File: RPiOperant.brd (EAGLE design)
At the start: 80 x 64 mm, 34 parts, among them IC1 74LS14N, IC3 MCP3008, J2 POWER_JACK, J3 POWER_JACK

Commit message: new board
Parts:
- removed D2: 1N4004, diode:DO41-10
- removed Q2: (no value), adafruit:TO220V
- removed R22, R23: 330, resistor:0207/7
- added IC2: 74LS14N, 74xx-us:DIL14
- added J1, J4: USB_B_PTH, SparkFun-Connectors:USB-B-PTH
- added J5, J6, J7, J8, J9: 1X2-3.5MM, adafruit:1X2-3.5MM
- added Q3, Q4, Q5, Q6: (no value), adafruit:TO220V
- added R24, R25, R26, R27, R28, R29: 1k, resistor:0207/7
- added R30, R31, R32, R33, R34, R35: 4.3k, resistor:0207/7
- added R36, R37, R38: 330, resistor:0207/7
- added U1: (no value), adafruit:TSSOP28
- added X2: (no value), con-subd:F25HP
- R17: value 1k -> 330
- moved R12 142.4 mm to (96.0, 45.0)
- moved R11 129.1 mm to (86.0, 50.0)
- moved SV1 126.0 mm to (131.0, 35.0), turned to 270 degrees
- moved R9 120.1 mm to (106.0, 40.0)
- moved R10 111.9 mm to (86.0, 40.0)
- moved SV2 70.0 mm to (5.00, 34.0), turned to 270 degrees
- moved Q1 64.0 mm to (43.0, 73.0)
- moved IC1 58.8 mm to (66.0, 58.0), turned to 0 degrees
- moved R17 55.8 mm to (96.0, 50.0)
- moved IC3 51.0 mm to (80.0, 28.0), turned to 0 degrees
- moved D1 50.8 mm to (17.0, 67.0), turned to 0 degrees
- moved R16 47.4 mm to (35.0, 67.0)
- moved R14 36.1 mm to (22.0, 43.0)
- moved X1 35.0 mm to (41.0, 88.0)
- moved R2 26.2 mm to (35.0, 58.0), turned to 0 degrees
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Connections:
- removed net GPIO2: SV1.3, SV2.3, X1.14
- removed net GPIO25: X1.18
- removed net GPIO3: SV1.5, SV2.5, X1.15
- removed net GPIO4: SV1.7, SV2.7
- removed net HOPPER_IR_LED: R12.1, X1.19
- removed net HOUSE_LIGHTS: D2.A, Q2.2, X1.5
- removed net IR_LED_C: R10.1, X1.21
- removed net IR_LED_L: R9.1, X1.22
- removed net IR_LED_R: R11.1, X1.20
- removed net LIGHTS_TRIG_GPIO: R17.1, SV1.32, SV2.32
- new net AUX1: J5.1, SV1.7, X2.1
- new net AUX2: J5.2, SV1.32, X2.2
- new net AUX3: J6.1, X2.3
- new net AUX4: J6.2, X2.4
- new net CENTNER_LED: R36.1
- new net GPIO18: J9.2, SV1.12
- new net HOUSELIGHT_B: Q4.2, X1.20
- new net HOUSELIGHT_B_GPIO: Q4.1, U1.8
- new net HOUSELIGHT_G: Q5.2, X1.21
- new net HOUSELIGHT_G_GPIO: Q5.1, U1.7
- new net HOUSELIGHT_R: Q3.2, X1.22
- new net HOUSELIGHT_R_GPIO: Q3.1, U1.6
- new net HOUSELIGHT_W: Q6.2, X1.19
- new net HOUSELIGHT_W_GPIO: Q6.1, U1.9
- new net IR_3: R24.1, R30.1, X2.23
- new net IR_3_GPIO: IC2.12, SV1.22, SV2.22
- new net IR_4: R25.1, R31.1, X2.22
- new net IR_4_GPIO: IC2.10, SV1.38
- new net IR_5: R26.1, R32.1, X2.21
- new net IR_5_GPIO: IC2.8, SV1.40
- new net IR_6: R27.1, R33.1, X2.20
- new net IR_6_GPIO: IC2.2, SV1.35, SV2.35
- new net IR_7: R28.1, R34.1
- new net IR_8: R29.1, R35.1
- new net LED_1: R38.1, X2.13
- new net LED_2: R9.1, X2.12
- new net LED_3: R10.1, X2.11
- new net LED_4: R11.1, X2.10
- new net LED_5: R12.1, X2.9
- new net LED_6: R21.1, X2.8
- new net LOADCELL2A+: X2.16
- new net LOADCELL2A-: X2.15
- new net LOADCELLA+: X1.15
- new net LOADCELLA-: X1.14
- new net LOADCELLE+: X1.25
- new net LOADCELLE-: X1.24
- new net N$11: IC2.5, R29.2
- new net N$13: R17.2, U1.10
- new net N$14: R36.2, U1.11
- new net N$15: R37.2, U1.12
- new net N$16: R38.2, U1.13
- new net N$17: IC2.4
- new net N$18: IC2.6
- new net N$26: R9.2, U1.15
- new net N$28: R11.2, U1.17
- new net N$29: R12.2, U1.18
- new net N$3: IC2.13, R24.2
- new net N$30: R21.2, U1.19
- new net N$4: IC2.11, R25.2
- new net N$5: IC2.9, R26.2
- new net N$7: IC2.1, R27.2
- new net N$9: IC2.3, R28.2
- new net RGB_CUE_B: X1.4
- new net RGB_CUE_G: X1.3
- new net RGB_CUE_R: X1.5
- new net RXD: J7.2, SV1.10
- new net SCL: SV1.5, U1.26
- new net SDA: SV1.3, U1.27
- new net TEMP: X1.2
- new net TXD: J7.1, SV1.8
- new net USB1_D+: J1.D+, X1.16
- new net USB1_D-: J1.D-, X1.17
- new net USB1_VBUS: J1.VBUS, X1.18
- new net USB2_D+: J4.D+, X2.17
- new net USB2_D-: J4.D-, X2.18
- new net USB2_VBUS: J4.VBUS, X2.19
- net +3V3: now also IC2.14, R30.2, R31.2, R32.2, R33.2, R34.2, R35.2, U1.1, U1.28, U1.3, U1.5; no longer R10.2, R11.2, R12.2, R9.2
- net +5V: no longer X1.25
- net 12V: no longer D2.C, X1.24
- net ADC0: now also X1.1; no longer X1.2
- net ADC1: now also X2.14; no longer X1.1
- net ADC2: now also X2.7; no longer X1.17
- net ADC3: now also X2.6
- net ADC4: now also X2.5; no longer X1.16
- net CENTER_LED: no longer R22.1
- net GND: now also IC2.7, J1.GND, J1.SHLD1, J1.SHLD2, J4.GND, J4.SHLD1, J4.SHLD2, Q3.3, Q4.3, Q5.3, Q6.3, U1.14, U1.2, U1.23, U1.24, U1.25, U1.4, X2.G1, X2.G2; no longer Q2.3
- net GPIO17: now also J9.1; no longer R23.1
- net GPIO22: now also J8.2; no longer R21.1
- net GPIO27: now also J8.1; no longer R22.2
- net IR_1: now also X2.25; no longer X1.4
- net IR_2: now also X2.24; no longer X1.3
- net LEFT_LED: now also R17.1; no longer R23.2
- net N$27: now also R10.2, U1.16; no longer Q2.1, R17.2
- net RIGHT_LED: now also R37.1; no longer R21.2
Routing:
- net +3V3: track 74.8 -> 262.4 mm, vias 0 -> 4
- net IR_6_GPIO: track 0.00 -> 179.9 mm, vias 0 -> 3
- net IR_6: track 0.00 -> 178.5 mm, vias 0 -> 2
- net GPIO17: track 79.0 -> 249.1 mm, vias 3 -> 2
- net IR_2_GPIO: track 0.00 -> 169.5 mm, vias 0 -> 3
- net IR_3_GPIO: track 0.00 -> 168.1 mm, vias 0 -> 4
- net AUX2: track 0.00 -> 153.0 mm, vias 0 -> 3
- net ADC2: track 25.7 -> 176.7 mm
- net AUX1: track 0.00 -> 147.7 mm, vias 0 -> 3
- net GPIO2: track 147.2 -> 0.00 mm, vias 2 -> 0
- net GPIO3: track 132.9 -> 0.00 mm, vias 2 -> 0
- net IR_4: track 0.00 -> 130.2 mm, vias 0 -> 3
- net IR_3: track 0.00 -> 128.7 mm, vias 0 -> 3
- net USB1_D+: track 0.00 -> 123.4 mm, vias 0 -> 2
- net ADC0: track 15.3 -> 130.4 mm
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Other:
- board size 80 x 64 mm -> 136 x 100 mm
- board text removed: "GENTNER LAB OPiRANT INTERFACE BRAD THEILMAN + TIM SAINBURG"

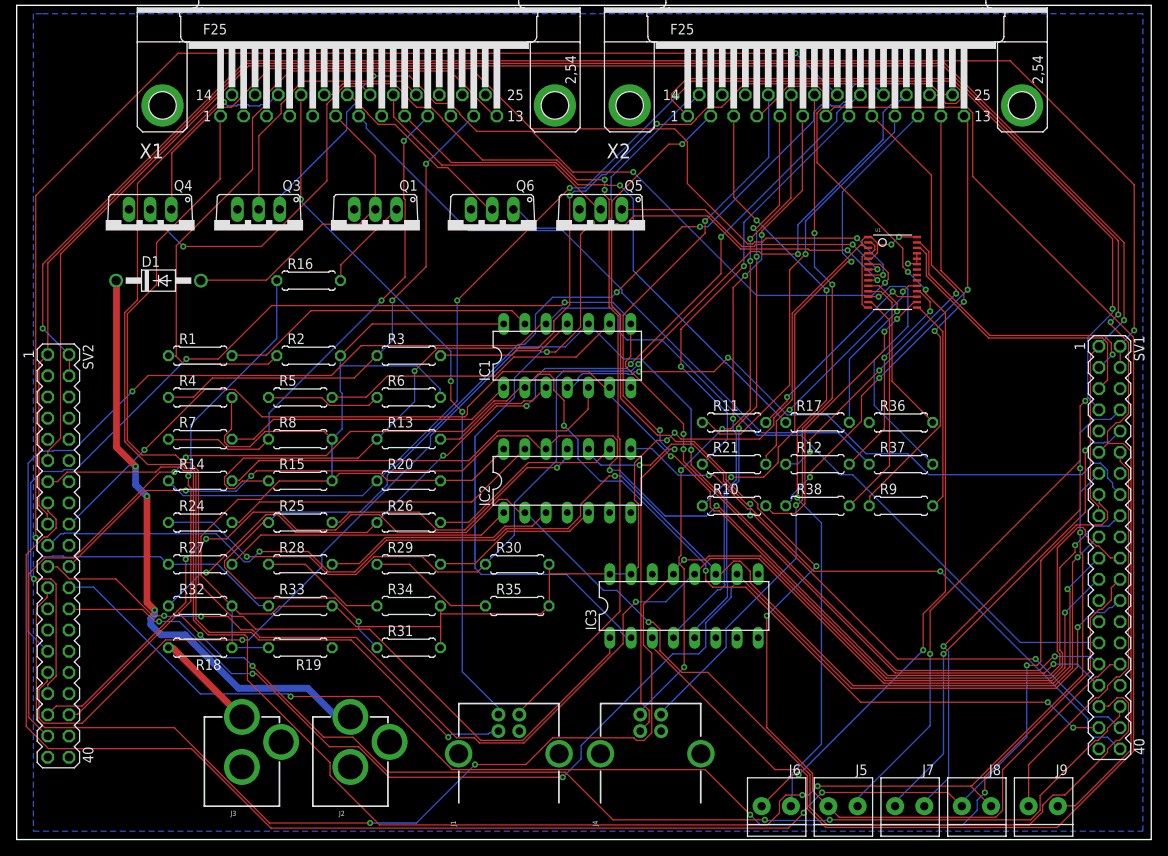
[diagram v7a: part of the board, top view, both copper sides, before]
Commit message: board labesl
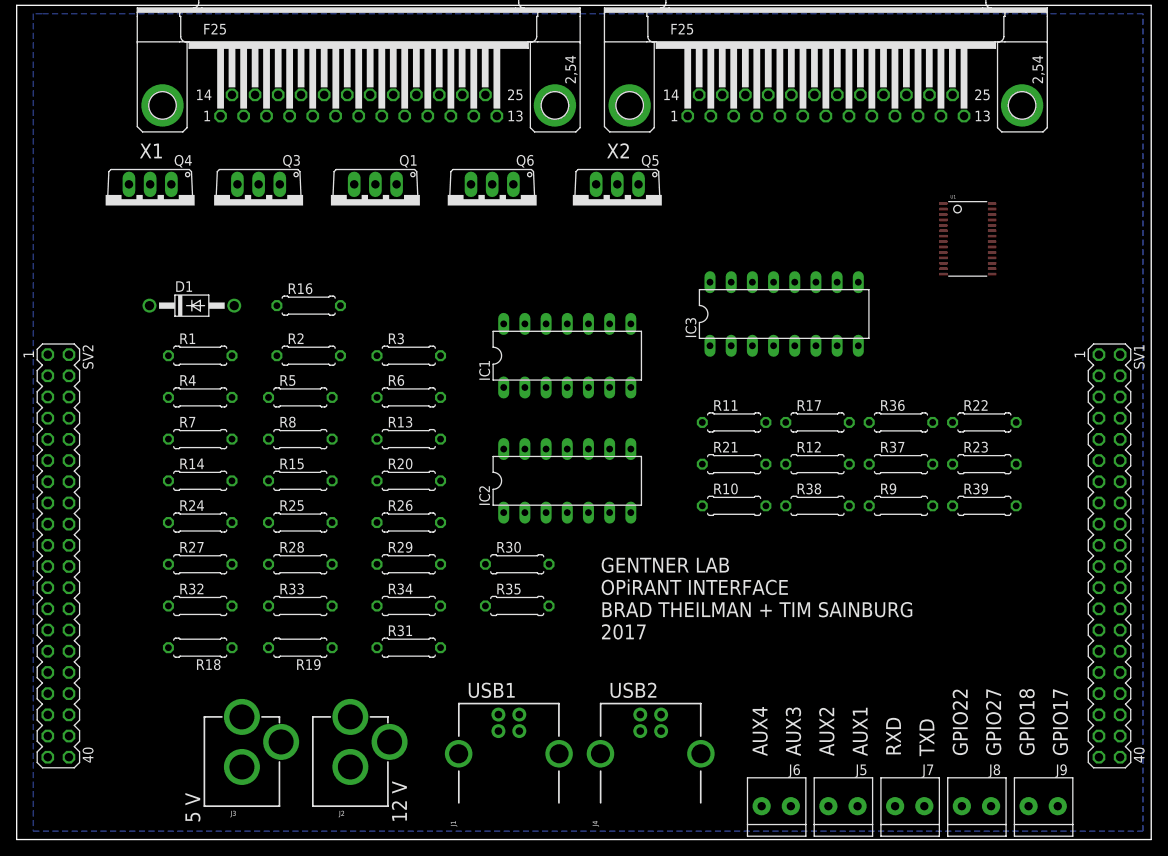
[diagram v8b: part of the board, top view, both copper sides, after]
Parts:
- added R22, R23, R39: 330, resistor:0207/7
- moved IC3 37.0 mm to (92.0, 63.0)
- moved U1 9.85 mm to (114.0, 72.0)
- moved D1 5.00 mm to (21.0, 64.0)
- moved Q5 3.61 mm to (72.0, 76.0)
- moved Q1 3.00 mm to (43.0, 76.0)
- moved Q3 3.00 mm to (29.0, 76.0)
- moved Q4 3.00 mm to (16.0, 76.0)
- moved Q6 3.00 mm to (57.0, 76.0)
- moved R16 3.00 mm to (35.0, 64.0)
- moved SV1 1.00 mm to (131.0, 34.0)
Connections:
- new net N$19: R22.2, U1.20
- new net N$20: R23.2, U1.21
- new net N$21: R39.2, U1.22
- net RGB_CUE_B: now also R39.1
- net RGB_CUE_G: now also R23.1
- net RGB_CUE_R: now also R22.1
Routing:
- net +3V3: track 262.4 -> 0.00 mm, vias 4 -> 0
- net GPIO17: track 249.1 -> 0.00 mm, vias 2 -> 0
- net RPI_3.3V: track 214.9 -> 0.00 mm, vias 1 -> 0
- net GPIO22: track 196.2 -> 0.00 mm, vias 3 -> 0
- net HOPPER_TRIG_GPIO: track 193.9 -> 0.00 mm, vias 5 -> 0
- net GPIO27: track 193.6 -> 0.00 mm, vias 3 -> 0
- net CENTER_PECK_GPIO: track 191.9 -> 0.00 mm, vias 6 -> 0
- net SCLK: track 188.2 -> 0.00 mm, vias 4 -> 0
- net RPI_5V: track 184.4 -> 0.00 mm, vias 2 -> 0
- net RIGHT_PECK_GPIO: track 181.4 -> 0.00 mm, vias 6 -> 0
- net IR_6_GPIO: track 179.9 -> 0.00 mm, vias 3 -> 0
- net IR_6: track 178.5 -> 0.00 mm, vias 2 -> 0
- net HOPPER_IR_GPIO: track 177.6 -> 0.00 mm, vias 1 -> 0
- net LEFT_PECK_GPIO: track 176.9 -> 0.00 mm, vias 3 -> 0
- net ADC2: track 176.7 -> 0.00 mm
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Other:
- board text added: "12 V"
- board text added: "5 V"
- board text added: "AUX1"
- board text added: "AUX2"
- board text added: "AUX3"
- board text added: "AUX4"
- board text added: "GENTNER LAB OPiRANT INTERFACE BRAD THEILMAN + TIM SAINBURG 2017"
- board text added: "GPIO17"
- board text added: "GPIO18"
- board text added: "GPIO22"
- board text added: "GPIO27"
- board text added: "RXD"
- board text added: "TXD"
- board text added: "USB1"
- board text added: "USB2"
